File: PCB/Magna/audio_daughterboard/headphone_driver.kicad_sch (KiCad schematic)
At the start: 41 parts, among them J601 AudioJack3, U601 NE5532, U602 NE5532, U603 TDA2822D

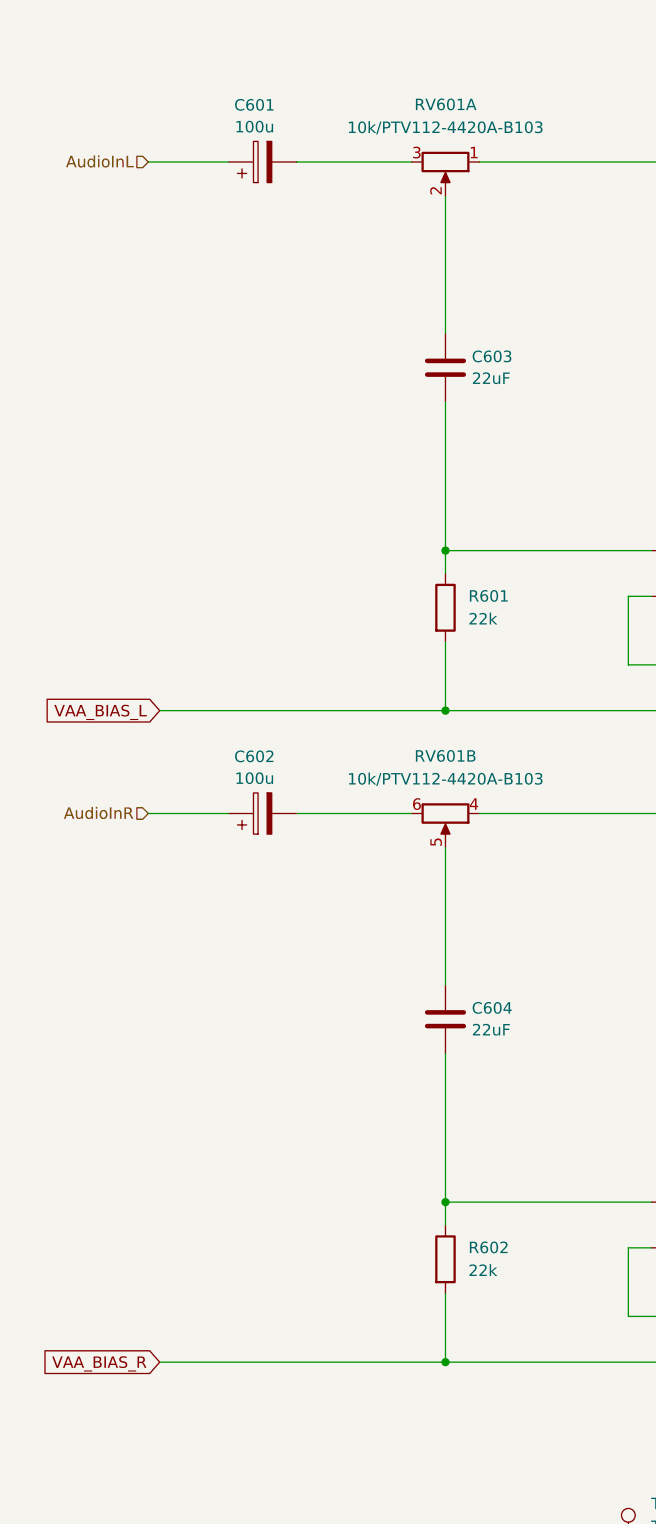
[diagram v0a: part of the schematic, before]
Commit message: Do most of the component placement for audio board
Just a general layout, things will probably change
as the routing begins.
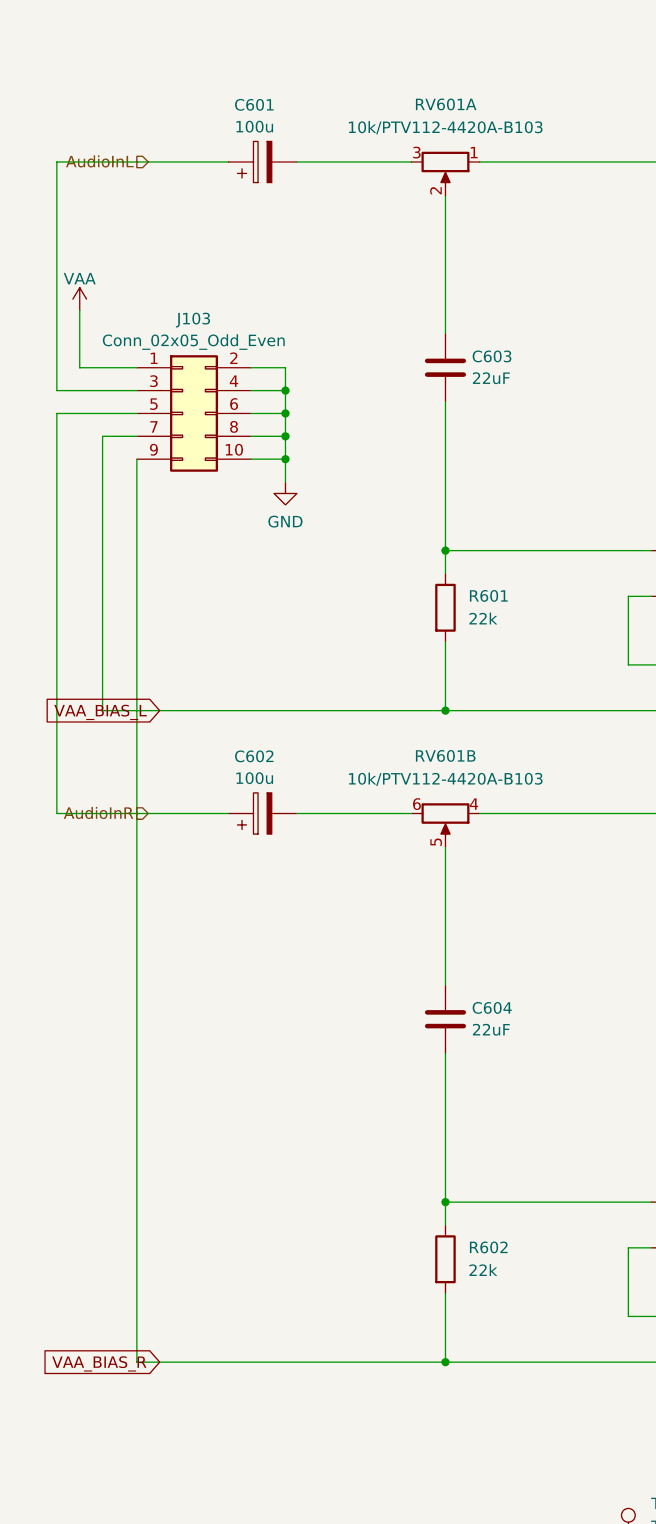
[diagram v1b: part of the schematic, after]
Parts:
- added J103: Conn_02x05_Odd_Even, Connector_PinHeader_2.54mm:PinHeader_2x05_P2.54mm_Horizontal, symbol Connector_Generic:Conn_02x05_Odd_Even
- C601, C602, C609, C610, C614, C615: footprint Capacitor_SMD:CP_Elec_6.3x5.8 -> Capacitor_SMD:CP_Elec_6.3x7.7; LCSC C2166157 -> C251007
- C607, C608: LCSC C2165067 -> C729680
- C611, C613, C616, C617: footprint Capacitor_SMD:C_0805_2012Metric_Pad1.18x1.45mm_HandSolder -> Capacitor_SMD:C_0603_1608Metric; LCSC C49678 -> C14663
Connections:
- net AudioInL: now also J103.3 (Pin_3)
- net AudioInR: now also J103.5 (Pin_5)
- net GND: now also J103.10 (Pin_10), J103.2 (Pin_2), J103.4 (Pin_4), J103.6 (Pin_6), J103.8 (Pin_8)
- net VAA: now also J103.1 (Pin_1)
- net VAA_BIAS_L: now also J103.7 (Pin_7)
- net VAA_BIAS_R: now also J103.9 (Pin_9)
